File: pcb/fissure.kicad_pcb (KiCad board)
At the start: 2 copper layers, 100 x 98 mm, 43 parts, among them J1 AudioJack4, J2 AudioJack4, K1 KEYSW, K10 KEYSW, K11 KEYSW, K12 KEYSW, K13 KEYSW, K14 KEYSW, K15 KEYSW, K16 KEYSW, K17 KEYSW, K18 KEYSW, K2 KEYSW, K3 KEYSW, K4 KEYSW, K5 KEYSW, K6 KEYSW, K7 KEYSW, K8 KEYSW, K9 KEYSW, U1 NRF24L01_Breakout, U2 BAT-HLD-001-THM, U3 ProMicro, U4 BAT-HLD-001-THM

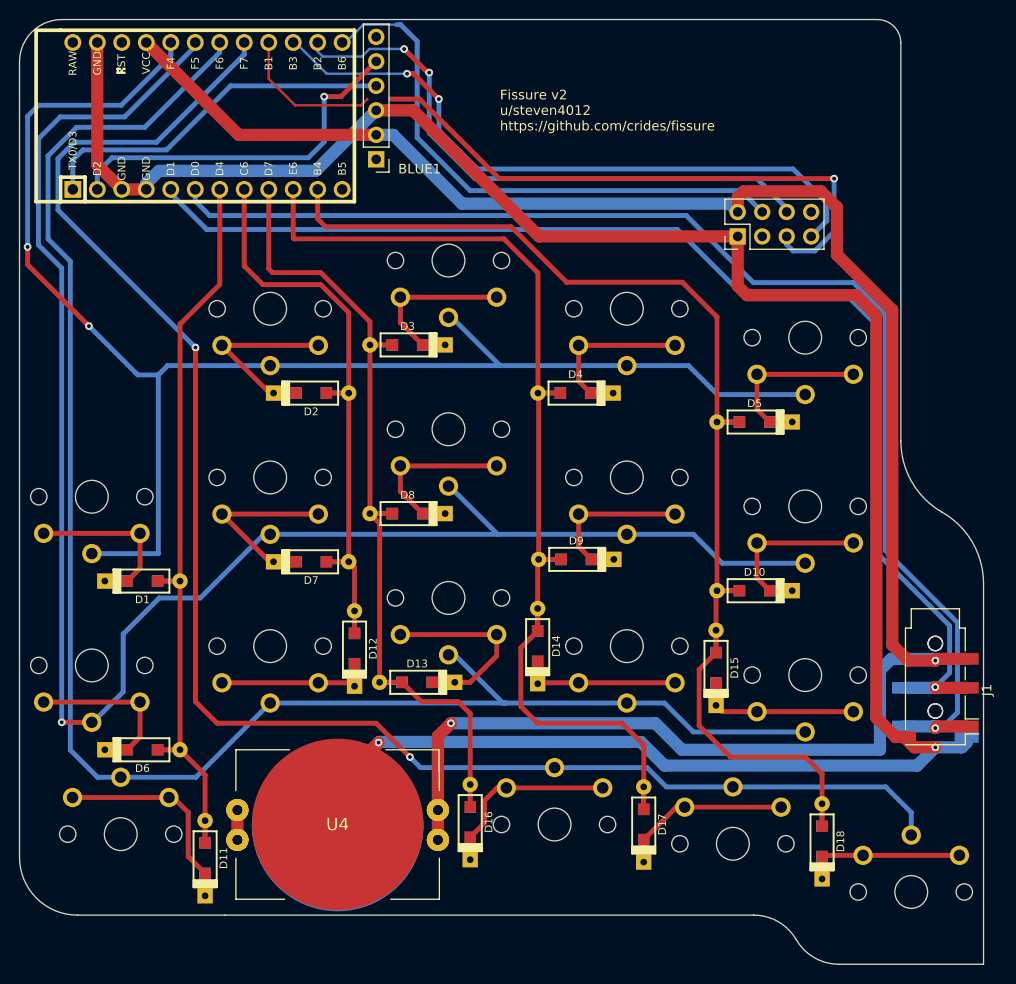
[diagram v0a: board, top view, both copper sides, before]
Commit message: Footprint fixes
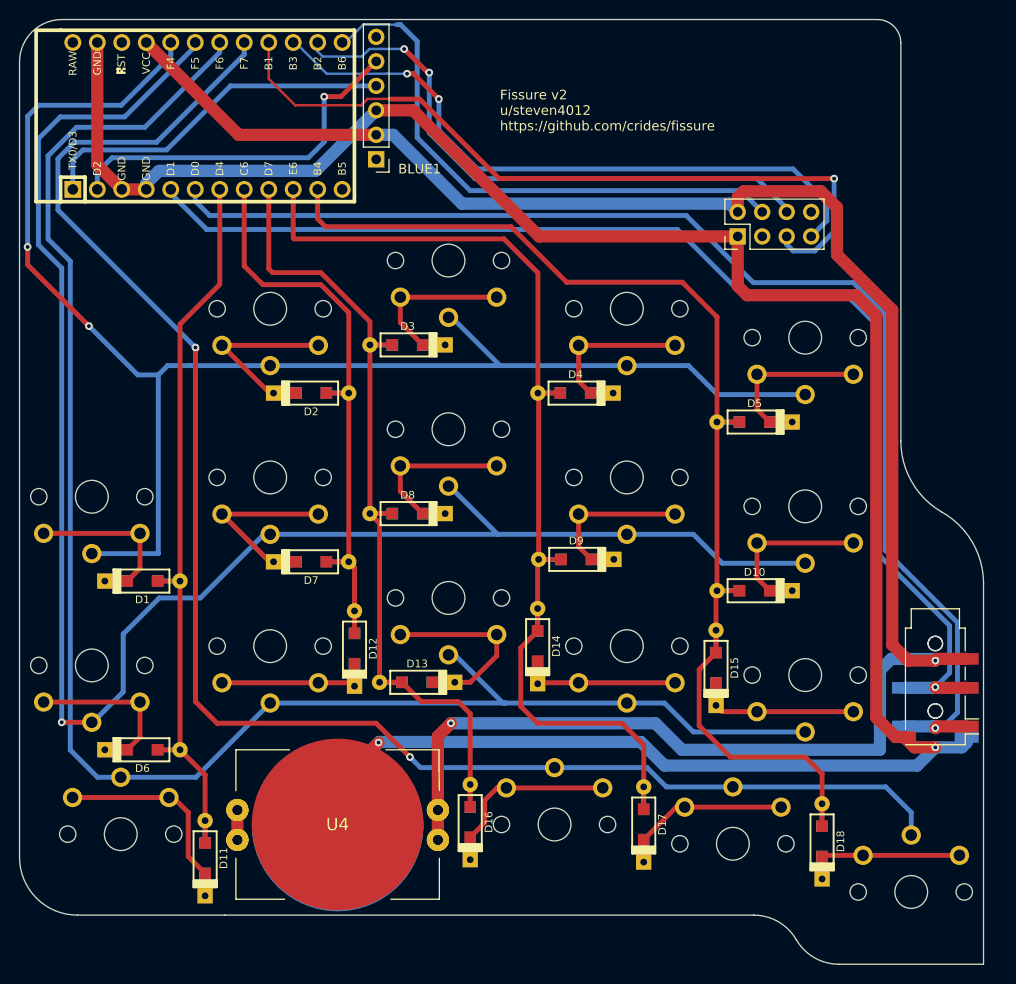
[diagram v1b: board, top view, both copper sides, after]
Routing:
- net SCLK: track 77.2 -> 79.6 mm

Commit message: Update README and PCB files
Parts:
- BLUE1: value Conn_01x06 -> Conn_01x04; footprint Connector_PinHeader_2.54mm:PinHeader_1x06_P2.54mm_Vertical -> misc:HC06
- moved D18 79.2 mm to (121.7, 43.0), turned to 180 degrees
- moved D17 77.3 mm to (105.2, 43.0), turned to 180 degrees
- moved D16 77.0 mm to (91.4, 43.0), turned to 180 degrees
- moved D13 60.3 mm to (91.4, 45.5)
- moved D15 58.8 mm to (121.7, 45.5), turned to 180 degrees
- moved D11 58.6 mm to (51.7, 66.2)
- moved D14 56.7 mm to (105.2, 45.5), turned to 180 degrees
- moved D10 48.0 mm to (121.7, 48.0)
- moved D6 46.9 mm to (49.2, 66.2), turned to 90 degrees
- moved D9 44.9 mm to (105.2, 48.0)
- moved D12 42.9 mm to (55.0, 66.2)
- moved D8 40.6 mm to (91.4, 48.0)
- moved D7 31.6 mm to (57.5, 66.2), turned to 90 degrees
- moved D1 30.4 mm to (46.7, 66.2), turned to 90 degrees
- moved D5 28.0 mm to (121.7, 50.5)
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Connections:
- BLUE1 pad 1: (no net) -> VCC
- BLUE1 pad 2: VCC -> GND
- BLUE1 pad 3: GND -> TX
- BLUE1 pad 4: TX -> RX
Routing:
- net Net-(D18-Pad1): track 14.3 -> 93.3 mm
- net Net-(D17-Pad1): track 15.6 -> 89.0 mm
- net Net-(D16-Pad1): track 17.6 -> 86.3 mm
- net Net-(D15-Pad1): track 14.5 -> 69.4 mm
- net Net-(D14-Pad1): track 14.3 -> 66.2 mm
- net VCC: track 213.5 -> 263.3 mm
- net GND: track 243.5 -> 289.1 mm, vias 2 -> 3
- net COL3: track 74.6 -> 29.2 mm
- net COL1: track 68.3 -> 24.4 mm
- net Net-(D10-Pad1): track 15.5 -> 58.4 mm
- net COL4: track 94.6 -> 51.8 mm
- net Net-(D13-Pad1): track 17.7 -> 60.1 mm
- net COL5: track 108.2 -> 65.9 mm
- net Net-(D11-Pad1): track 20.1 -> 60.3 mm
- net COL2: track 53.2 -> 17.1 mm
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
